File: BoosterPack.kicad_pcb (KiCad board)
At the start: 2 copper layers, 61 parts, among them IC1 LTC4372IMS8#TRPBF, IC2 L4940D2T12-TR, IC3 MAX738ACWE+, IC4 PJ-002A, IC5 DRV103U_2K5, J1 691137710002, J2 PRT-16763, J3 691137710002, J4 53048-0810, Q1 BSC026NE2LS5ATMA1

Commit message: Preliminary Board Layout, no ground plane or traces yet
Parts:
- moved Q1 109.6 mm to (171.4, 68.6)
- moved R4 108.3 mm to (118.1, 124.5), turned to 270 degrees
- moved J4 103.7 mm to (102.9, 43.2), turned to 180 degrees
- moved C1 100.0 mm to (184.2, 59.7)
- moved J1 99.0 mm to (176.5, 47.0), turned to 0 degrees
- moved IC1 98.3 mm to (162.6, 69.8)
- moved R1 98.3 mm to (163.8, 63.5), turned to 90 degrees
- moved C4 86.9 mm to (147.3, 69.8), turned to 270 degrees
- moved TP10 85.2 mm to (152.4, 142.2)
- moved TP7 84.6 mm to (189.2, 45.7)
- moved C2 84.2 mm to (153.7, 69.8), turned to 270 degrees
- moved IC4 84.0 mm to (154.9, 57.1), turned to 270 degrees
- moved TP5 83.1 mm to (121.9, 108.0)
- moved D1 81.8 mm to (156.2, 63.5), turned to 180 degrees
- moved TP11 78.1 mm to (133.3, 142.2)
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
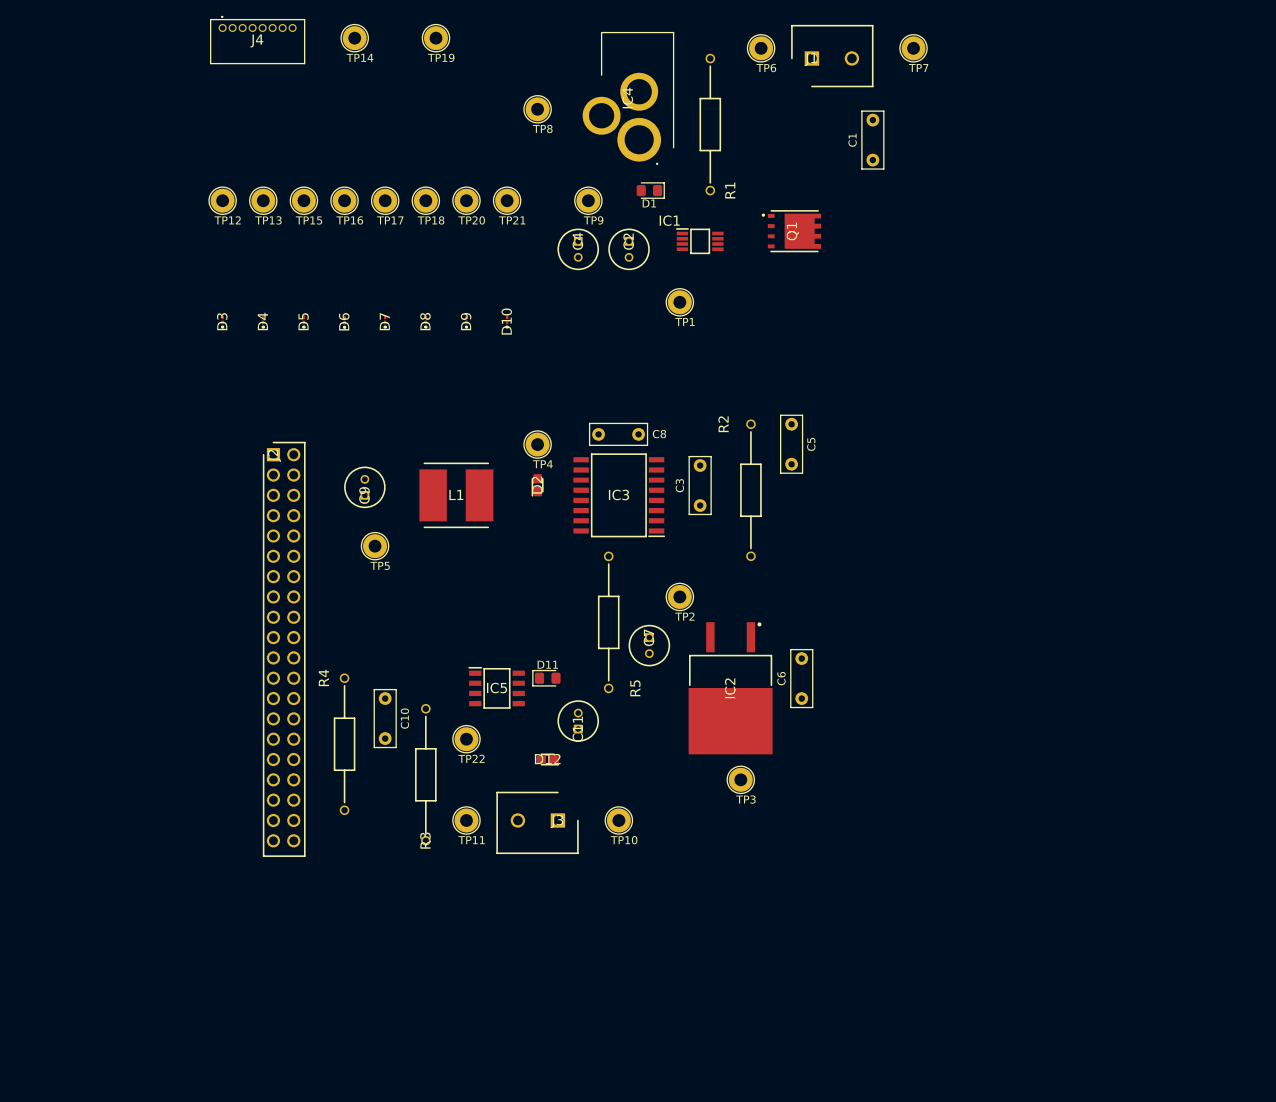
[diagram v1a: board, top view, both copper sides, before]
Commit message: Added all traces except 1 trace that needs a via and all connections to ground
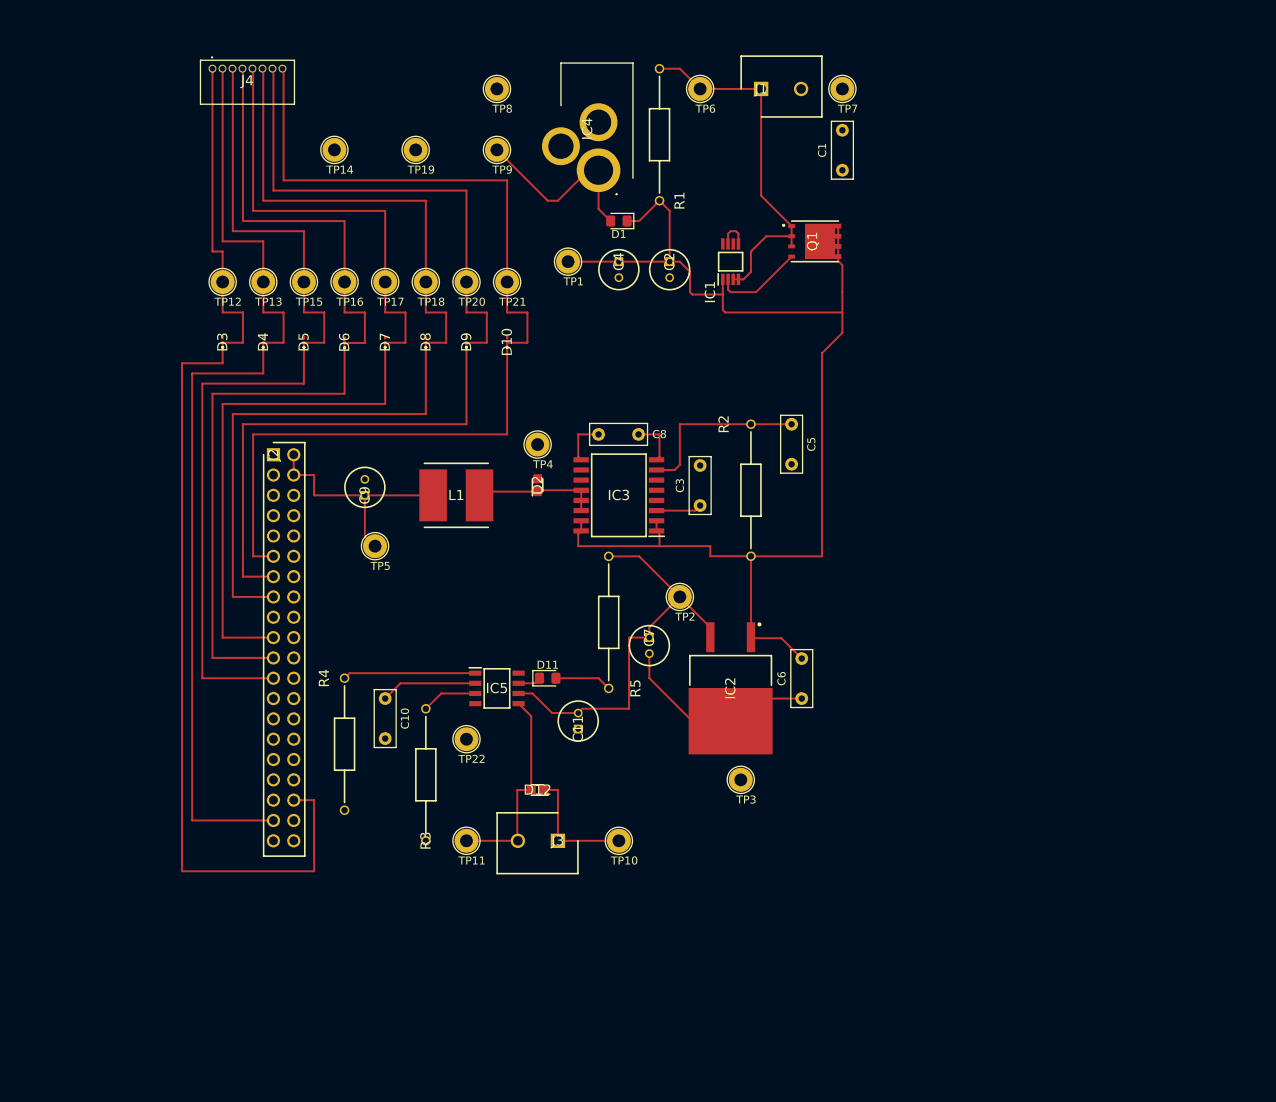
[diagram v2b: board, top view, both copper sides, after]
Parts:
- moved TP1 14.9 mm to (146.1, 72.4)
- moved TP14 14.2 mm to (116.8, 58.4)
- moved TP19 14.2 mm to (127.0, 58.4)
- moved TP9 13.1 mm to (137.2, 58.4)
- moved TP7 10.2 mm to (180.3, 50.8)
- moved TP12 10.2 mm to (102.9, 74.9)
- moved TP13 10.2 mm to (108.0, 74.9)
- moved TP15 10.2 mm to (113.0, 74.9)
- moved TP16 10.2 mm to (118.1, 74.9)
- moved TP17 10.2 mm to (123.2, 74.9)
- moved TP18 10.2 mm to (128.3, 74.9)
- moved TP20 10.2 mm to (133.3, 74.9)
- moved TP21 10.2 mm to (138.4, 74.9)
- moved TP6 9.16 mm to (162.6, 50.8)
- moved J1 7.41 mm to (170.2, 50.8)
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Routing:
- net Net-(C2-Pad1): track 0.00 -> 153.2 mm
- net Net-(D3-Pad1): track 0.00 -> 139.7 mm
- net Net-(D10-Pad1): track 0.00 -> 128.3 mm
- net Net-(D9-Pad1): track 0.00 -> 124.6 mm
- net Net-(D4-Pad1): track 0.00 -> 123.2 mm
- net Net-(D8-Pad1): track 0.00 -> 120.7 mm
- net Net-(D7-Pad1): track 0.00 -> 119.4 mm
- net Net-(D6-Pad1): track 0.00 -> 115.6 mm
- net Net-(D5-Pad1): track 0.00 -> 111.8 mm
- net /Connectors/VS: track 0.00 -> 66.4 mm
- net /Connectors/Rechargeable_Batteries: track 0.00 -> 46.0 mm
- net /Connectors/5V_Reg: track 0.00 -> 35.2 mm
- net /Connectors/Control: track 0.00 -> 26.0 mm
- net GND: track 0.00 -> 25.5 mm
- net /Connectors/VCC: track 0.00 -> 23.9 mm
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
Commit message: Finished first attempt at routing
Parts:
- added H1: MountingHole, MountingHole:MountingHole_2.7mm_M2.5_Pad, F.Cu at (177.8, 135.9)
- added H2: MountingHole, MountingHole:MountingHole_2.7mm_M2.5_Pad, F.Cu at (156.2, 135.9)
- added H3: MountingHole, MountingHole:MountingHole_2.7mm_M2.5_Pad, F.Cu at (156.2, 85.1)
- added H4: MountingHole, MountingHole:MountingHole_2.7mm_M2.5_Pad, F.Cu at (177.8, 85.1)
- moved TP4 19.0 mm to (142.2, 114.3)
- moved R5 17.0 mm to (135.1, 119.9), turned to 0 degrees
- moved C1 13.2 mm to (167.1, 60.5), turned to 270 degrees
- moved IC2 0.90 mm to (167.0, 125.1)
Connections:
- IC3 pad 10: Net-(IC3-Pad10) -> GND
- IC3 pad 11: Net-(IC3-Pad10) -> GND
- Q1 pad 9: Net-(Q1-Pad9) -> Net-(C2-Pad1)
- TP19 pad 1: Net-(TP19-Pad1) -> GND
- TP22 pad 1: Net-(TP22-Pad1) -> GND
- TP3 pad 1: Net-(TP3-Pad1) -> GND
- TP4 pad 1: Net-(TP4-Pad1) -> GND
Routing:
- net /Connectors/Solenoid_Driver_Input: track 0.00 -> 36.7 mm
- net GND: track 25.5 -> 58.4 mm, vias 0 -> 10
- net Net-(C2-Pad1): track 153.2 -> 127.2 mm
- net Net-(D3-Pad1): track 139.7 -> 118.4 mm
- net Net-(D6-Pad1): track 115.6 -> 94.5 mm
- net Net-(D7-Pad1): track 119.4 -> 98.5 mm
- net Net-(D5-Pad1): track 111.8 -> 91.0 mm
- net Net-(D10-Pad1): track 128.3 -> 107.7 mm
- net Net-(D8-Pad1): track 120.7 -> 100.6 mm
- net Net-(D9-Pad1): track 124.6 -> 104.7 mm
- net /Connectors/5V_Reg: track 35.2 -> 54.5 mm
- net Net-(D4-Pad1): track 123.2 -> 106.3 mm
- net Net-(D11-Pad2): track 7.12 -> 12.3 mm
- net Net-(C1-Pad2): track 4.13 -> 9.00 mm
- net Net-(C8-Pad2): track 5.95 -> 4.11 mm
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- added copper zone on B.Cu, net GND
- added copper zone on F.Cu, net Net-(C2-Pad1)
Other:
- board outline added: 88.9 x 107.9 mm

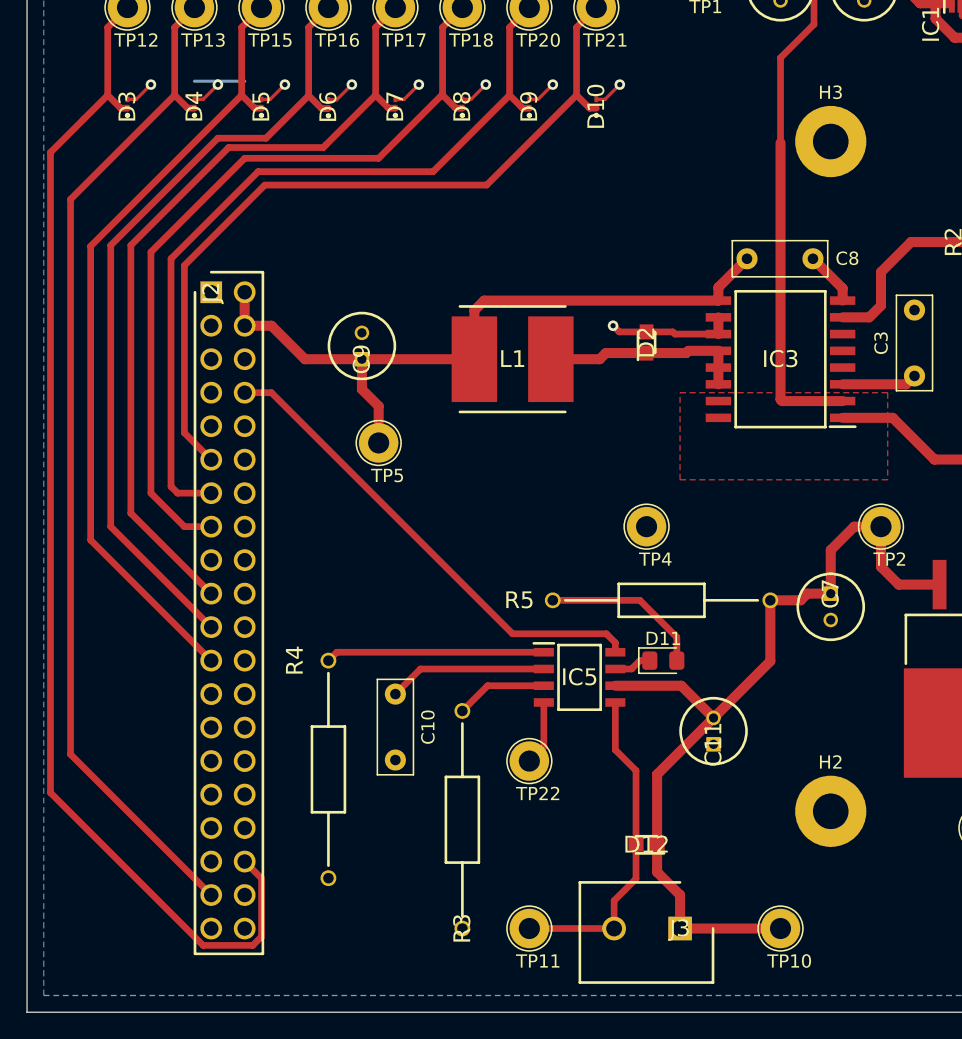
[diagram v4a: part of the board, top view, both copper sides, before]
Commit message: Board Layout Revisions: moved left two mounting holes a couple mm to right, moved trace connected to Pin 36 of Pi a little bit
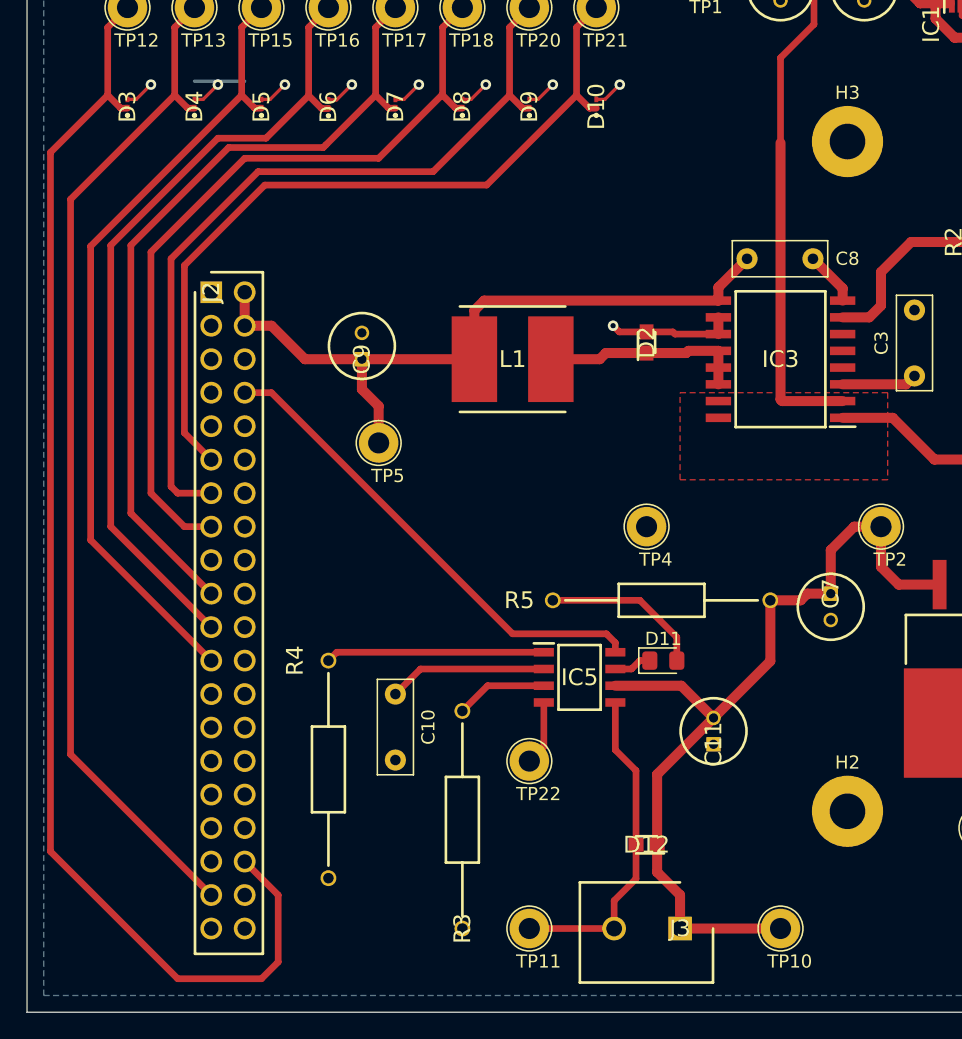
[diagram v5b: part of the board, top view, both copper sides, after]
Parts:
- moved H2 1.27 mm to (157.5, 135.9)
- moved H3 1.27 mm to (157.5, 85.1)
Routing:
- net Net-(D3-Pad1): track 118.4 -> 126.0 mm
